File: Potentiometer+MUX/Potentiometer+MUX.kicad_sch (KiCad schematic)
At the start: 9 parts

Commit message: Layout + Schem Update
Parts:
- added C1, C2, C3, C4, C5, C6, C7, C8, C9: 0.1uF, Capacitor_THT:C_Disc_D5.0mm_W2.5mm_P2.50mm, symbol Device:C_Small
- added J1: Conn_01x04, Connector_PinHeader_2.54mm:PinHeader_1x04_P2.54mm_Horizontal, symbol Connector_Generic:Conn_01x04
- added J2: Conn_01x02, Connector_PinHeader_2.54mm:PinHeader_1x02_P2.54mm_Horizontal, symbol Connector_Generic:Conn_01x02
- added J3: Conn_01x08, Connector_PinHeader_2.54mm:PinHeader_1x08_P2.54mm_Vertical, symbol Connector_Generic:Conn_01x08
- added J4: Conn_01x16, Connector_PinSocket_2.54mm:PinSocket_1x16_P2.54mm_Vertical, symbol Connector_Generic:Conn_01x16
- RV1, RV2, RV3, RV4, RV5, RV6, RV7, RV8: footprint (none) -> Potentiometer_THT:Potentiometer_Omeg_PC16BU_Vertical
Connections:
- net +3.3V: now also C1.1, C2.1, C3.1, C4.1, C5.1, C6.1, C7.1, C8.1, C9.1, J2.1 (Pin_1), J3.2 (Pin_2)
- net GND: now also C1.2, C2.2, C3.2, C4.2, C5.2, C6.2, C7.2, C8.2, C9.2, J2.2 (Pin_2), J3.1 (Pin_1), J3.3 (Pin_3)
- net at MUX1. (GND), RV2.2: now also J4.15 (Pin_15)
- net at MUX1. (GND), RV5.2: now also J4.12 (Pin_12)
- net at MUX1. (GND), RV8.2: now also J4.9 (Pin_9)
- net at MUX1. (GND), RV1.2: now also J4.16 (Pin_16)
- net at MUX1. (GND), RV3.2: now also J4.14 (Pin_14)
- net at MUX1. (GND), RV6.2: now also J4.11 (Pin_11)
- net at MUX1. (GND), RV7.2: now also J4.10 (Pin_10)
- net at MUX1. (GND), RV4.2: now also J4.13 (Pin_13)
- new net: J1.1 (Pin_1), J3.8 (Pin_8), MUX1. (GND)
- new net: J1.2 (Pin_2), J3.6 (Pin_6), MUX1. (GND)
- new net: J1.3 (Pin_3), J3.5 (Pin_5), MUX1. (GND)
- new net: J1.4 (Pin_4), J3.4 (Pin_4), MUX1. (GND)
- no-connect marks 0 -> 18
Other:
- moved on the sheet: MUX1, RV1, RV2, RV3, RV4, RV5, RV6, RV7, RV8

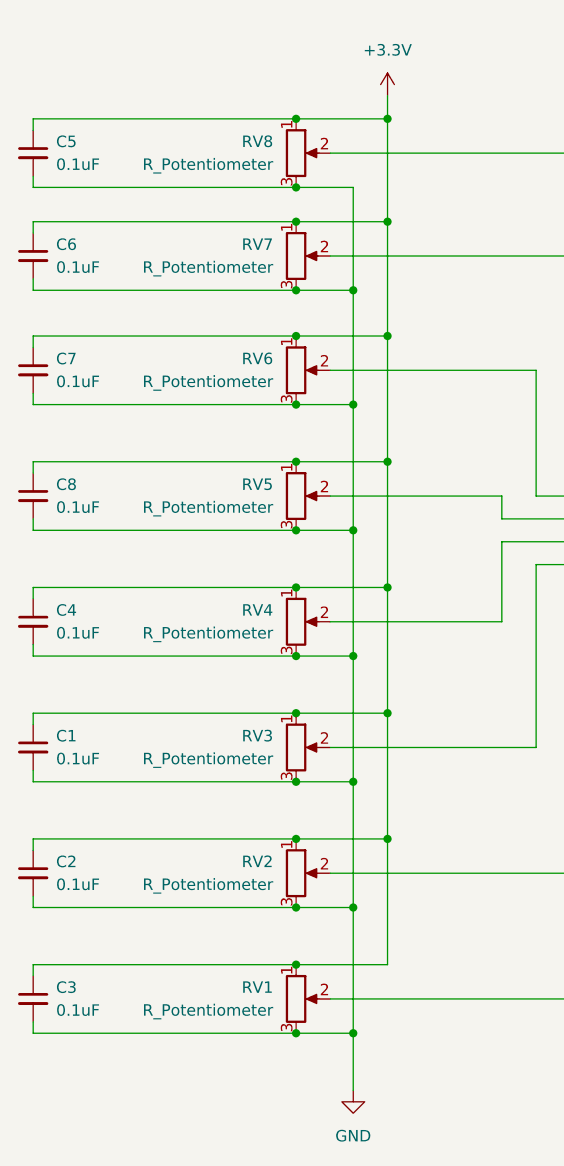
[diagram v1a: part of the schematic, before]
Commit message: Smaller MUX, Main Board design
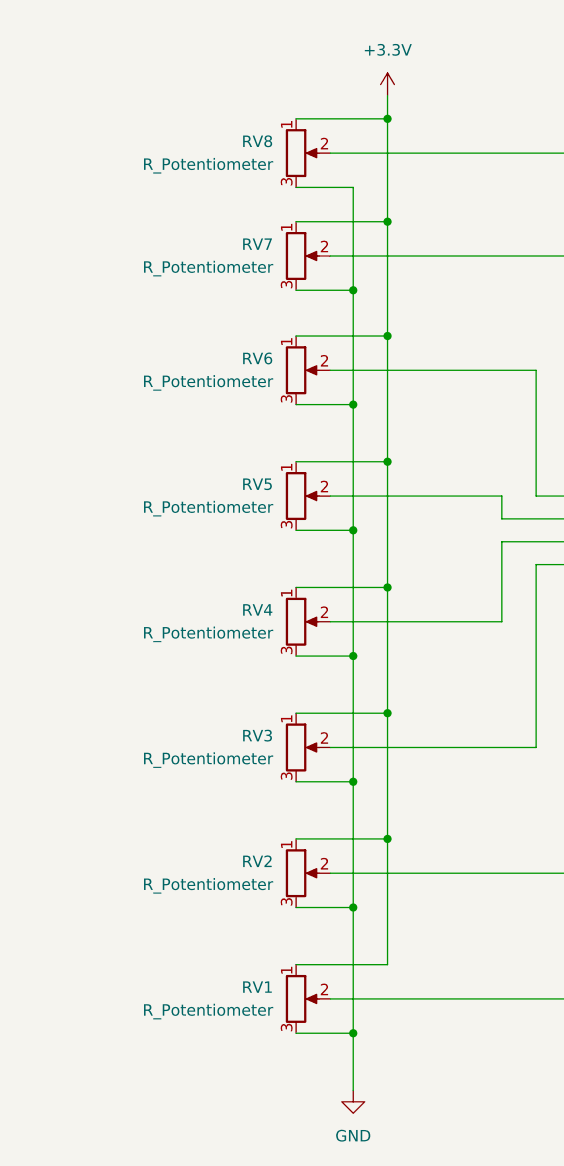
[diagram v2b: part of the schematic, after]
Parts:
- removed C1, C2, C3, C4, C5, C6, C7, C8: 0.1uF, Capacitor_THT:C_Disc_D5.0mm_W2.5mm_P2.50mm, symbol Device:C_Small
